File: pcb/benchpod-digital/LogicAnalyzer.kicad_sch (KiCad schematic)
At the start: 54 parts, among them U18 SN74LVC2G66DCUR, U19 SN74LVC2G66DCUR, U20 SN74LVC2G66DCUR, U21 SN74LVC2G66DCUR, U22 SRV05-4.TCT, U23 SRV05-4.TCT, U25 SRV05-4.TCT, U34 SRV05-4.TCT, U54 TCA9554PWR

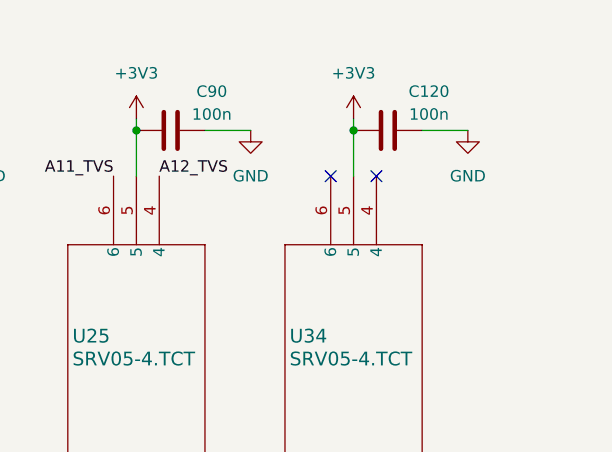
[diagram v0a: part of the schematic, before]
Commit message: digital v3r3: carry over the analog v3r2 schematic changes
Same refs and nets as analog v3r1 in these areas, so the v3r2 fixes map 1:1.

- RoHS: D3 SS34 C8678 -> C3014011, D5 SMAJ20A C41376408 -> C5353170.
- U4 ESP32-C3-MINI-1-H4 (C2934569): the N4 is out of stock at JLC; same
  module, footprint and chip, 105 C rated.
- Package shrinks (whole BOM lines, no new lines): 8.2p C29/C30/C50/C51 and
  3.3n C99/C102/C119/C226 0603 -> 0402, 2.2u C218/C219 1206 -> 0603.
- EMC: D11 spare channels on USB CC1/CC2, U34 spares on +1V8 and LA_VCCIO.
- Debug: H1 (SWD 2x5) and H3 (HEADER1) removed; J10 SWO/NRST/SWCLK/SWDIO and
  J11 USART2_RX/+3V3/GND/USART2_TX 2x2, both DNP; PB3 = SWO, PD5/PD6 = USART2.

Not carried over: the 0.1 % resistors (on analog they only share lines with
the ADC parts) and the R164 revision strap (stays 1k: firmware runs the
digital board as v3). The PCB still needs Update PCB from Schematic.

Co-Authored-By: Claude Opus 5.5 <noreply@anthropic.com>
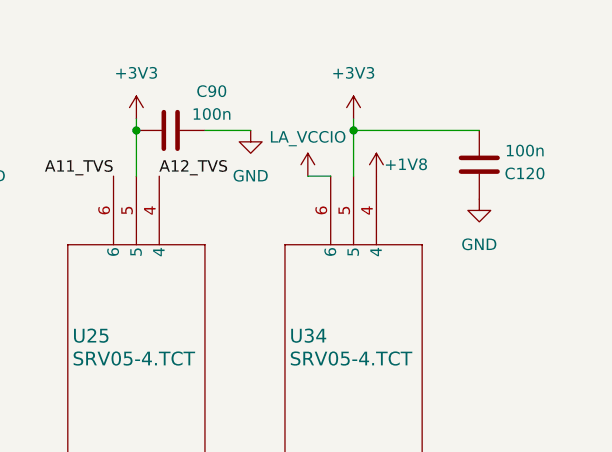
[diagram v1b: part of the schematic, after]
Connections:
- net +3V3: now also C120.2; no longer C120.1
- net GND: now also C120.1; no longer C120.2
- net LA_VCCIO: now also U34.6
- net +1V8: now reaches U34.4
- no-connect marks 2 -> 0
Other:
- moved on the sheet: C120
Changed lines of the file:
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@@
 	)
 	(junction
-		(at 256.54 33.02)
-		(diameter 0)
-		(color 0 0 0 0)
-	)
-	(junction
 		(at 78.74 157.48)
 		(diameter 0)
@@
 	)
 	(junction
+		(at 256.54 33.02)
+		(diameter 0)
+		(color 0 0 0 0)
+	)
+	(junction
 		(at 110.49 130.81)
 		(diameter 0)
@@
 		(color 0 0 0 0)
 	)
-	(no_connect
-		(at 254 38.1)
-	)
-	(no_connect
-		(at 259.08 38.1)
-	)
 	(wire
 		(pts
@@
 	(wire
 		(pts
+			(xy 251.46 38.1) (xy 254 38.1)
+		)
+		(stroke
+			(width 0)
+			(type default)
+		)
+	)
+	(wire
+		(pts
 			(xy 66.04 129.54) (xy 66.04 135.89)
 		)
@@
 	(wire
 		(pts
-			(xy 269.24 33.02) (xy 264.16 33.02)
-		)
-		(stroke
-			(width 0)
-			(type default)
-		)
-	)
-	(wire
-		(pts
 			(xy 139.7 125.73) (xy 138.43 125.73)
 		)
@@
 	(wire
 		(pts
+			(xy 256.54 33.02) (xy 270.51 33.02)
+		)
+		(stroke
+			(width 0)
+			(type default)
+		)
+	)
+	(wire
+		(pts
 			(xy 60.96 157.48) (xy 60.96 170.18)
 		)
@@
 	)
 	(symbol
+		(lib_id "power:+3V3")
+		(at 251.46 38.1 0)
+		(unit 1)
+		(body_style 1)
+		(exclude_from_sim no)
+		(in_bom yes)
+		(on_board yes)
+		(in_pos_files yes)
+		(dnp no)
+		(property "Reference" "#PWR0449"
+			(at 251.46 41.91 0)
+			(hide yes)
+			(show_name no)
+			(do_not_autoplace no)
+			(effects
+				(font
+					(size 1.27 1.27)
+				)
+			)
+		)
+		(property "Value" "LA_VCCIO"
+			(at 251.46 33.782 0)
+			(show_name no)
+			(do_not_autoplace no)
+			(effects
+				(font
+					(size 1.27 1.27)
+				)
+			)
+		)
+		(property "Footprint" ""
+			(at 251.46 38.1 0)
+			(hide yes)
+			(show_name no)
+			(do_not_autoplace no)
+			(effects
+				(font
+					(size 1.27 1.27)
+				)
+			)
+		)
+		(property "Datasheet" ""
+			(at 251.46 38.1 0)
+			(hide yes)
+			(show_name no)
+			(do_not_autoplace no)
+			(effects
+				(font
+					(size 1.27 1.27)
+				)
+			)
+		)
+		(property "Description" "Power symbol creates a global label with name \"+3V3\""
+			(at 251.46 38.1 0)
+			(hide yes)
+			(show_name no)
+			(do_not_autoplace no)
+			(effects
+				(font
+					(size 1.27 1.27)
+				)
+			)
+		)
+		(pin "1"
+		)
+		(instances
+			(project "vbench-pod"
+				(path "/745fcf4b-2e0b-4fc4-95c0-f2e3fd40beb9/e3454fef-24e2-422b-9513-46b286a60c18"
+					(reference "#PWR0449")
+					(unit 1)
+				)
+			)
+		)
+	)
+	(symbol
 		(lib_id "Device:R")
 		(at 162.56 132.08 0)
@@
 	(symbol
 		(lib_id "power:GND")
-		(at 269.24 33.02 0)
+		(at 270.51 40.64 0)
 		(unit 1)
 		(body_style 1)
@@
 		(fields_autoplaced yes)
 		(property "Reference" "#PWR0202"
-			(at 269.24 39.37 0)
+			(at 270.51 46.99 0)
 			(hide yes)
 			(show_name no)
@@
 		)
 		(property "Value" "GND"
-			(at 269.24 38.1 0)
+			(at 270.51 45.72 0)
 			(show_name no)
 			(do_not_autoplace no)
@@
 		)
 		(property "Footprint" ""
-			(at 269.24 33.02 0)
+			(at 270.51 40.64 0)
 			(hide yes)
 			(show_name no)
@@
 		)
 		(property "Datasheet" ""
-			(at 269.24 33.02 0)
+			(at 270.51 40.64 0)
 			(hide yes)
 			(show_name no)
@@
 		)
 		(property "Description" "Power symbol creates a global label with name \"GND\" , ground"
-			(at 269.24 33.02 0)
+			(at 270.51 40.64 0)
 			(hide yes)
 			(show_name no)
@@
 	(symbol
 		(lib_id "Device:C")
-		(at 260.35 33.02 90)
+		(at 270.51 36.83 180)
 		(unit 1)
 		(body_style 1)
@@
 		(dnp no)
 		(property "Reference" "C120"
-			(at 264.922 28.702 90)
+			(at 275.59 37.846 0)
 			(show_name no)
 			(do_not_autoplace no)
@@
 		)
 		(property "Value" "100n"
-			(at 264.922 31.242 90)
+			(at 275.59 35.306 0)
 			(show_name no)
 			(do_not_autoplace no)
@@
 		)
 		(property "Footprint" "Capacitor_SMD:C_0402_1005Metric"
-			(at 264.16 32.0548 0)
+			(at 269.5448 33.02 0)
 			(hide yes)
 			(show_name no)
@@
 		)
 		(property "Datasheet" ""
-			(at 260.35 33.02 0)
+			(at 270.51 36.83 0)
 			(hide yes)
 			(show_name no)
@@
 		)
 		(property "Description" "Unpolarized capacitor"
-			(at 260.35 33.02 0)
+			(at 270.51 36.83 0)
 			(hide yes)
 			(show_name no)
@@
 		)
 		(property "LCSC" "C307331"
-			(at 260.35 33.02 90)
+			(at 270.51 36.83 90)
 			(hide yes)
 			(show_name no)
@@
 		)
 		(property "LCSC Part #" ""
-			(at 260.35 33.02 90)
+			(at 270.51 36.83 90)
 			(hide yes)
 			(show_name no)
@@
 		)
 		(property "MFR. Part #" ""
-			(at 260.35 33.02 90)
+			(at 270.51 36.83 90)
 			(hide yes)
 			(show_name no)
@@
 		)
 		(property "KiLib_Generator" "SMD_2terminal_chip_molded"
-			(at 260.35 33.02 0)
+			(at 270.51 36.83 0)
 			(hide yes)
 			(show_name no)
@@
 		)
 		(property "Arrow Part Number" ""
-			(at 260.35 33.02 90)
+			(at 270.51 36.83 90)
 			(hide yes)
 			(show_name no)
@@
 		)
 		(property "Arrow Price/Stock" ""
-			(at 260.35 33.02 90)
+			(at 270.51 36.83 90)
 			(hide yes)
 			(show_name no)
@@
 		)
 		(property "Height" ""
-			(at 260.35 33.02 90)
+			(at 270.51 36.83 90)
 			(hide yes)
 			(show_name no)
@@
 		)
 		(property "Manufacturer_Name" ""
-			(at 260.35 33.02 90)
+			(at 270.51 36.83 90)
 			(hide yes)
 			(show_name no)
@@
 		)
 		(property "Manufacturer_Part_Number" ""
-			(at 260.35 33.02 90)
+			(at 270.51 36.83 90)
 			(hide yes)
 			(show_name no)
@@
 		)
 		(property "Mouser Part Number" ""
-			(at 260.35 33.02 90)
+			(at 270.51 36.83 90)
 			(hide yes)
 			(show_name no)
@@
 		)
 		(property "Mouser Price/Stock" ""
-			(at 260.35 33.02 90)
+			(at 270.51 36.83 90)
 			(hide yes)
 			(show_name no)
@@
 		)
 		(property "ProductID" ""
-			(at 260.35 33.02 90)
+			(at 270.51 36.83 90)
 			(hide yes)
 			(show_name no)
@@
 		)
 		(property "Sim.Pins" ""
-			(at 260.35 33.02 90)
+			(at 270.51 36.83 90)
 			(hide yes)
 			(show_name no)
@@
 		)
 		(property "KLC_S3.3" ""
-			(at 260.35 33.02 90)
+			(at 270.51 36.83 90)
 			(hide yes)
 			(show_name no)
@@
 		)
 		(property "KLC_S4.1" ""
-			(at 260.35 33.02 90)
+			(at 270.51 36.83 90)
 			(hide yes)
 			(show_name no)
@@
 					(unit 1)
 				)
+			)
+		)
+	)
+	(symbol
+		(lib_id "power:+3V3")
+		(at 259.08 38.1 0)
+		(unit 1)
+		(body_style 1)
+		(exclude_from_sim no)
+		(in_bom yes)
+		(on_board yes)
+		(in_pos_files yes)
+		(dnp no)
+		(property "Reference" "#PWR0450"
+			(at 259.08 41.91 0)
+			(hide yes)
+			(show_name no)
+			(do_not_autoplace no)
+			(effects
+				(font
+					(size 1.27 1.27)
+				)
+			)
+		)
+		(property "Value" "+1V8"
+			(at 262.382 36.83 0)
+			(show_name no)
+			(do_not_autoplace no)
+			(effects
+				(font
+					(size 1.27 1.27)
+				)
+			)
+		)
+		(property "Footprint" ""
+			(at 259.08 38.1 0)
+			(hide yes)
+			(show_name no)
+			(do_not_autoplace no)
+			(effects
+				(font
+					(size 1.27 1.27)
+				)
+			)
+		)
+		(property "Datasheet" ""
+			(at 259.08 38.1 0)
+			(hide yes)
+			(show_name no)
+			(do_not_autoplace no)
+			(effects
+				(font
+					(size 1.27 1.27)
+				)
+			)
+		)
+		(property "Description" "Power symbol creates a global label with name \"+3V3\""
+			(at 259.08 38.1 0)
+			(hide yes)
+			(show_name no)
+			(do_not_autoplace no)
+			(effects
+				(font
+					(size 1.27 1.27)
+				)
+			)
+		)
+		(pin "1"
+		)
+		(instances
+			(project "vbench-pod"
+				(path "/745fcf4b-2e0b-4fc4-95c0-f2e3fd40beb9/e3454fef-24e2-422b-9513-46b286a60c18"
+					(reference "#PWR0450")
+					(unit 1)
+				)

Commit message: digital v3r3: C120 back to its v3r2 orientation (pad 1 = +3V3) so the existing traces fit
Co-Authored-By: Claude Opus 5.5 <noreply@anthropic.com>
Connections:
- net +3V3: now also C120.1; no longer C120.2
- net GND: now also C120.2; no longer C120.1
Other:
- moved on the sheet: C120
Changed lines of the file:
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@@
 	(symbol
 		(lib_id "Device:C")
-		(at 270.51 36.83 180)
+		(at 270.51 36.83 0)
 		(unit 1)
 		(body_style 1)
